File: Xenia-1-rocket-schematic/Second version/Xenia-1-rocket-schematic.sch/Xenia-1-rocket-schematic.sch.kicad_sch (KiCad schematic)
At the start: 0 parts

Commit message: Schematic back to october version
Back to where I was in october, with two sensors
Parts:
- added A?: ADA3708, ADA3708_RPI-ZERO, symbol ADA3708:ADA3708
- added U?: BME280, symbol Rocketry_project:BME280
- added U?: LSM9DS1, symbol Rocketry_project:LSM9DS1
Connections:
- new net: A?.1 (3V3[1]), U?.~ (V_in), U?.~ (V_in)
- new net: A?.3 (GPIO2/SDA), U?.~ (V_in)
- new net: A?.5 (GPIO3/SCL), U?.~ (V_in)
- new net: A?.11 (GPIO17/GEN0), U?.~ (V_in)
- new net: A?.13 (GPIO27/GEN2), U?.~ (V_in)
- new net GND: A?.9 (GND[1]), U?.~ (V_in), U?.~ (V_in)
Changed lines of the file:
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@@
 (kicad_sch (version 20211123) (generator eeschema)
   (paper "A4")
+  (junction (at 180.34 118.11) (diameter 0) (color 0 0 0 0)
+  )
+  (junction (at 163.83 69.85) (diameter 0) (color 0 0 0 0)
+  )
+  (junction (at 168.91 133.35) (diameter 0) (color 0 0 0 0)
+  )
+  (wire (pts (xy 93.98 88.9) (xy 96.52 88.9))
+    (stroke (width 0) (type default) (color 0 0 0 0))
+  )
+  (wire (pts (xy 213.36 125.73) (xy 93.98 125.73))
+    (stroke (width 0) (type default) (color 0 0 0 0))
+  )
+  (wire (pts (xy 88.9 133.35) (xy 88.9 83.82))
+    (stroke (width 0) (type default) (color 0 0 0 0))
+  )
+  (wire (pts (xy 152.4 69.85) (xy 163.83 69.85))
+    (stroke (width 0) (type default) (color 0 0 0 0))
+  )
+  (wire (pts (xy 88.9 83.82) (xy 96.52 83.82))
+    (stroke (width 0) (type default) (color 0 0 0 0))
+  )
+  (wire (pts (xy 91.44 76.2) (xy 96.52 76.2))
+    (stroke (width 0) (type default) (color 0 0 0 0))
+  )
+  (wire (pts (xy 163.83 104.14) (xy 163.83 69.85))
+    (stroke (width 0) (type default) (color 0 0 0 0))
+  )
+  (wire (pts (xy 91.44 129.54) (xy 91.44 86.36))
+    (stroke (width 0) (type default) (color 0 0 0 0))
+  )
+  (wire (pts (xy 201.93 104.14) (xy 201.93 118.11))
+    (stroke (width 0) (type default) (color 0 0 0 0))
+  )
+  (wire (pts (xy 213.36 104.14) (xy 213.36 125.73))
+    (stroke (width 0) (type default) (color 0 0 0 0))
+  )
+  (wire (pts (xy 180.34 118.11) (xy 180.34 133.35))
+    (stroke (width 0) (type default) (color 0 0 0 0))
+  )
+  (wire (pts (xy 180.34 62.23) (xy 180.34 118.11))
+    (stroke (width 0) (type default) (color 0 0 0 0))
+  )
+  (wire (pts (xy 96.52 73.66) (xy 96.52 60.96))
+    (stroke (width 0) (type default) (color 0 0 0 0))
+  )
+  (wire (pts (xy 194.31 104.14) (xy 163.83 104.14))
+    (stroke (width 0) (type default) (color 0 0 0 0))
+  )
+  (wire (pts (xy 184.15 68.58) (xy 87.63 68.58))
+    (stroke (width 0) (type default) (color 0 0 0 0))
+  )
+  (wire (pts (xy 163.83 69.85) (xy 172.72 69.85))
+    (stroke (width 0) (type default) (color 0 0 0 0))
+  )
+  (wire (pts (xy 184.15 62.23) (xy 184.15 68.58))
+    (stroke (width 0) (type default) (color 0 0 0 0))
+  )
+  (wire (pts (xy 152.4 60.96) (xy 152.4 69.85))
+    (stroke (width 0) (type default) (color 0 0 0 0))
+  )
+  (wire (pts (xy 91.44 64.77) (xy 91.44 76.2))
+    (stroke (width 0) (type default) (color 0 0 0 0))
+  )
+  (wire (pts (xy 91.44 86.36) (xy 96.52 86.36))
+    (stroke (width 0) (type default) (color 0 0 0 0))
+  )
+  (wire (pts (xy 96.52 60.96) (xy 152.4 60.96))
+    (stroke (width 0) (type default) (color 0 0 0 0))
+  )
+  (wire (pts (xy 87.63 68.58) (xy 87.63 78.74))
+    (stroke (width 0) (type default) (color 0 0 0 0))
+  )
+  (wire (pts (xy 205.74 104.14) (xy 205.74 129.54))
+    (stroke (width 0) (type default) (color 0 0 0 0))
+  )
+  (wire (pts (xy 191.77 64.77) (xy 91.44 64.77))
+    (stroke (width 0) (type default) (color 0 0 0 0))
+  )
+  (wire (pts (xy 201.93 118.11) (xy 180.34 118.11))
+    (stroke (width 0) (type default) (color 0 0 0 0))
+  )
+  (wire (pts (xy 93.98 125.73) (xy 93.98 88.9))
+    (stroke (width 0) (type default) (color 0 0 0 0))
+  )
+  (wire (pts (xy 168.91 133.35) (xy 88.9 133.35))
+    (stroke (width 0) (type default) (color 0 0 0 0))
+  )
+  (wire (pts (xy 205.74 129.54) (xy 91.44 129.54))
+    (stroke (width 0) (type default) (color 0 0 0 0))
+  )
+  (wire (pts (xy 191.77 62.23) (xy 191.77 64.77))
+    (stroke (width 0) (type default) (color 0 0 0 0))
+  )
+  (wire (pts (xy 87.63 78.74) (xy 96.52 78.74))
+    (stroke (width 0) (type default) (color 0 0 0 0))
+  )
+  (wire (pts (xy 180.34 133.35) (xy 168.91 133.35))
+    (stroke (width 0) (type default) (color 0 0 0 0))
+  )
+  (wire (pts (xy 172.72 69.85) (xy 172.72 62.23))
+    (stroke (width 0) (type default) (color 0 0 0 0))
+  )
+  (symbol (lib_id "Rocketry_project:BME280") (at 180.34 52.07 0) (unit 1)
+    (in_bom yes) (on_board yes) (fields_autoplaced)
+    (property "Reference" "U?" (id 0) (at 202.565 52.5053 0)
+      (effects (font (size 1.27 1.27)) (justify left))
+    )
+    (property "Value" "BME280" (id 1) (at 202.565 55.0422 0)
+      (effects (font (size 1.27 1.27)) (justify left))
+    )
+    (property "Footprint" "" (id 2) (at 180.34 52.07 0)
+      (effects (font (size 1.27 1.27)) hide)
+    )
+    (property "Datasheet" "" (id 3) (at 180.34 52.07 0)
+      (effects (font (size 1.27 1.27)) hide)
+    )
+    (pin "~")
+    (pin "~")
+    (pin "~")
+    (pin "~")
+    (pin "~")
+    (pin "~")
+    (pin "~")
+  )
+  (symbol (lib_id "power:GND") (at 168.91 133.35 0) (unit 1)
+    (in_bom yes) (on_board yes) (fields_autoplaced)
+    (property "Reference" "#PWR?" (id 0) (at 168.91 139.7 0)
+      (effects (font (size 1.27 1.27)) hide)
+    )
+    (property "Value" "GND" (id 1) (at 168.91 137.7934 0))
+    (property "Footprint" "" (id 2) (at 168.91 133.35 0)
+      (effects (font (size 1.27 1.27)) hide)
+    )
+    (property "Datasheet" "" (id 3) (at 168.91 133.35 0)
+      (effects (font (size 1.27 1.27)) hide)
+    )
+    (pin "1")
+  )
+  (symbol (lib_id "ADA3708:ADA3708") (at 119.38 96.52 0) (unit 1)
+    (in_bom yes) (on_board yes) (fields_autoplaced)
+    (property "Reference" "A?" (id 0) (at 119.38 67.4202 0))
+    (property "Value" "ADA3708" (id 1) (at 119.38 69.9571 0))
+    (property "Footprint" "ADA3708_RPI-ZERO" (id 2) (at 119.38 96.52 0)
+      (effects (font (size 1.27 1.27)) (justify left bottom) hide)
+    )
+    (property "Datasheet" "" (id 3) (at 119.38 96.52 0)
+      (effects (font (size 1.27 1.27)) (justify left bottom) hide)
+    )
+    (property "MANUFACTURER" "Raspberry" (id 4) (at 119.38 96.52 0)
+      (effects (font (size 1.27 1.27)) (justify left bottom) hide)
+    )
+    (property "STANDARD" "MAnufactutrer Recommendations" (id 5) (at 119.38 96.52 0)
+      (effects (font (size 1.27 1.27)) (justify left bottom) hide)
+    )
+    (pin "1")
+    (pin "10")
+    (pin "11")
+    (pin "12")
+    (pin "13")
+    (pin "14")
+    (pin "15")
+    (pin "16")
+    (pin "17")
+    (pin "18")
+    (pin "19")
+    (pin "2")
+    (pin "20")
+    (pin "21")
+    (pin "22")
+    (pin "23")
+    (pin "24")
+    (pin "25")
+    (pin "26")
+    (pin "27")
+    (pin "28")
+    (pin "29")
+    (pin "3")
+    (pin "30")
+    (pin "31")
+    (pin "32")
+    (pin "33")
+    (pin "34")
+    (pin "35")
+    (pin "36")
+    (pin "37")
+    (pin "38")
+    (pin "39")
+    (pin "4")
+    (pin "40")
+    (pin "5")
+    (pin "6")
+    (pin "7")
+    (pin "8")
+    (pin "9")
+  )
+  (symbol (lib_id "Rocketry_project:LSM9DS1") (at 198.12 100.33 0) (unit 1)
+    (in_bom yes) (on_board yes) (fields_autoplaced)
+    (property "Reference" "U?" (id 0) (at 213.995 90.4072 0))
+    (property "Value" "LSM9DS1" (id 1) (at 213.995 92.9441 0))
+    (property "Footprint" "" (id 2) (at 204.47 95.25 0)
+      (effects (font (size 1.27 1.27)) hide)
+    )
+    (property "Datasheet" "" (id 3) (at 204.47 95.25 0)
+      (effects (font (size 1.27 1.27)) hide)
+    )
+    (pin "~")
+    (pin "~")
+    (pin "~")
+    (pin "~")
+    (pin "~")
+    (pin "~")
+    (pin "~")
+    (pin "~")
+    (pin "~")
+  )
   (sheet_instances
     (path "/" (page "1"))
   )
+  (symbol_instances
+    (path "/5b534168-8c44-4d39-b8ef-48b6953bd40d"
+      (reference "#PWR?") (unit 1) (value "GND") (footprint "")
+    )
+    (path "/82b31fed-6ca0-41f8-9a54-4771ef08f750"
+      (reference "A?") (unit 1) (value "ADA3708") (footprint "ADA3708_RPI-ZERO")
+    )
+    (path "/46adcbd4-74d0-4c16-b05f-98374f2f3ebf"
+      (reference "U?") (unit 1) (value "BME280") (footprint "")
+    )
+    (path "/ea1947e1-cd2e-46b0-a351-5a513277da19"
+      (reference "U?") (unit 1) (value "LSM9DS1") (footprint "")
+    )
+  )
 )

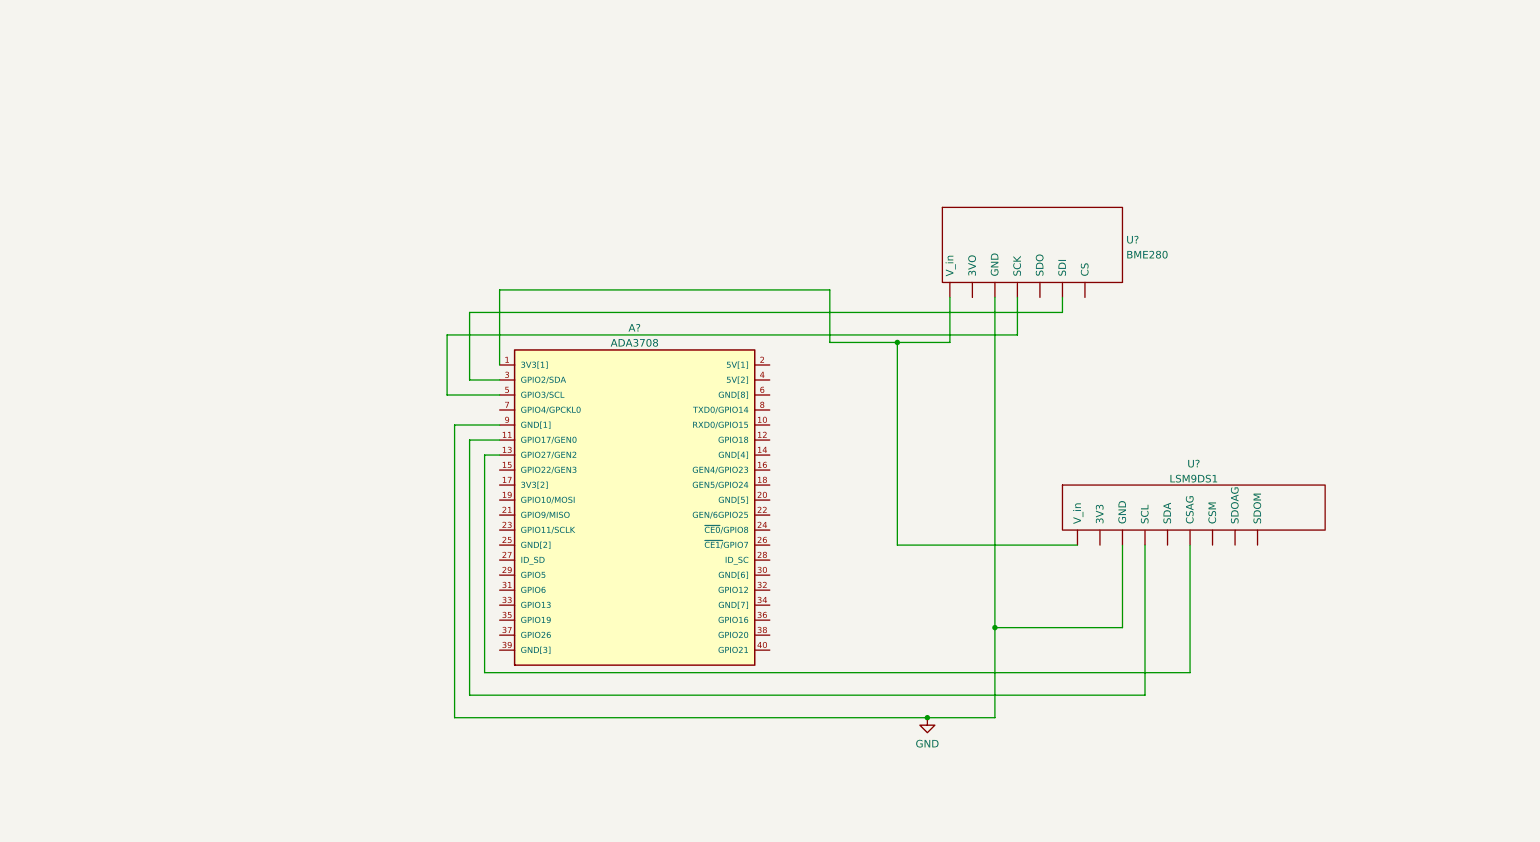
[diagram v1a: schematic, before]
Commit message: Added HX711 HDMI cable and wired it
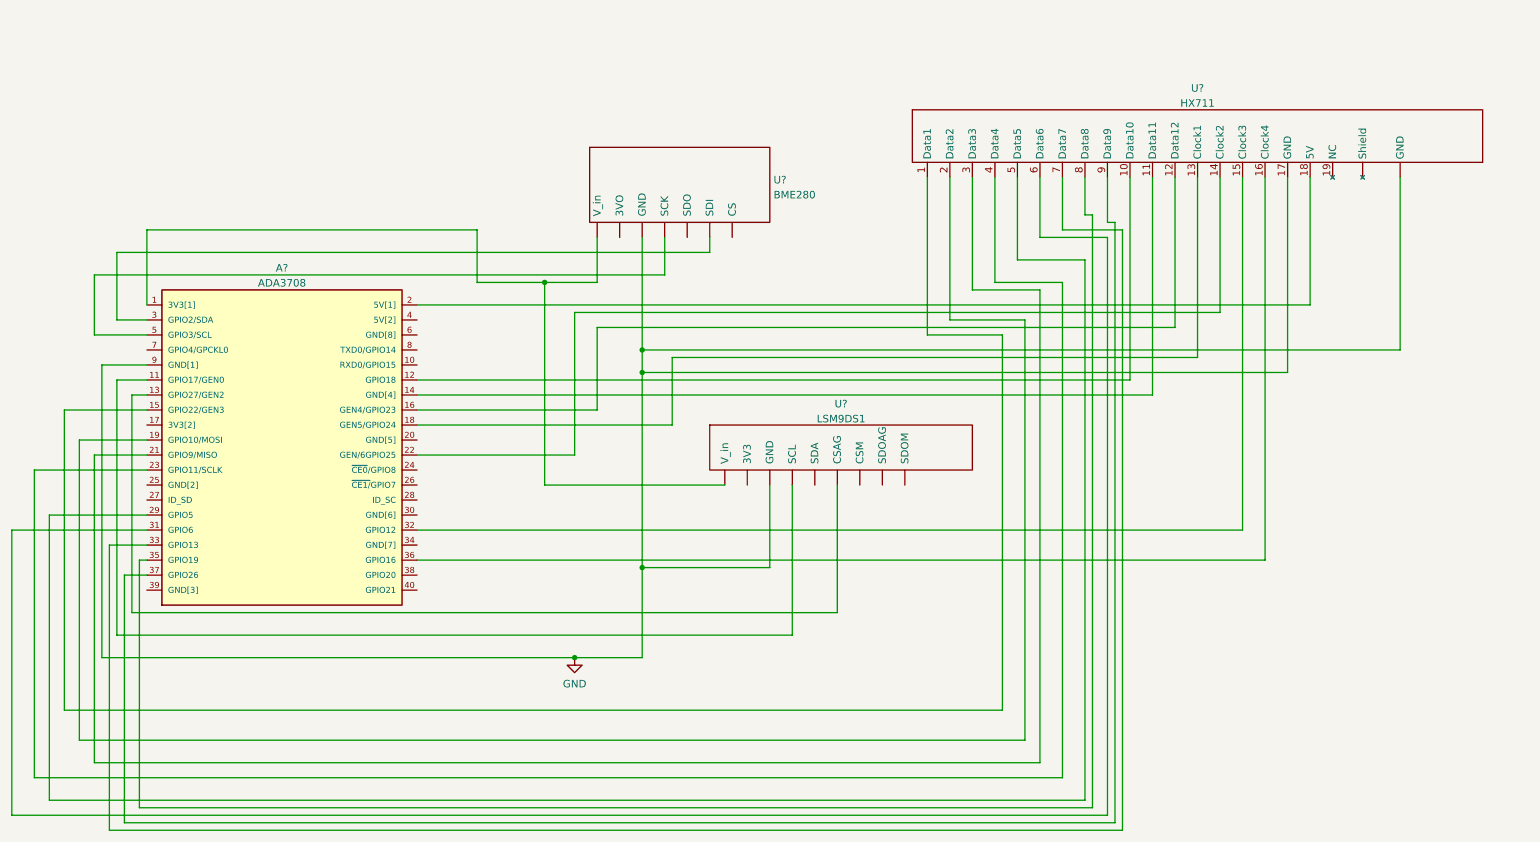
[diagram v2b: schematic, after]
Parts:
- added U?: HX711, symbol Rocketry_project:HX711
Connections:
- net GND: now also U?. (Shield), U?.17 (GND)
- net at A?.12 (GPIO18): now also U?.10 (Data10)
- net at A?.14 (GND[4]): now also U?.11 (Data11)
- net at A?.15 (GPIO22/GEN3): now also U?.1 (Data1)
- net at A?.16 (GEN4/GPIO23): now also U?.12 (Data12)
- net at A?.18 (GEN5/GPIO24): now also U?.13 (Clock1)
- net at A?.19 (GPIO10/MOSI): now also U?.2 (Data2)
- net at A?.2 (5V[1]): now also U?.18 (5V)
- net at A?.21 (GPIO9/MISO): now also U?.3 (Data3)
- net at A?.22 (GEN/6GPIO25): now also U?.14 (Clock2)
- net at A?.23 (GPIO11/SCLK): now also U?.4 (Data4)
- net at A?.29 (GPIO5): now also U?.5 (Data5)
- net at A?.31 (GPIO6): now also U?.6 (Data6)
- net at A?.32 (GPIO12): now also U?.15 (Clock3)
- net at A?.33 (GPIO13): now also U?.7 (Data7)
- net at A?.35 (GPIO19): now also U?.8 (Data8)
- net at A?.36 (GPIO16): now also U?.16 (Clock4)
- net at A?.37 (GPIO26): now also U?.9 (Data9)
- new net: A?.1 (3V3[1]), U?.~ (V_in), U?.~ (V_in)
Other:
- moved on the sheet: A?, U?

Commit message: Changing a list of symbols to labels
Small changes to labels
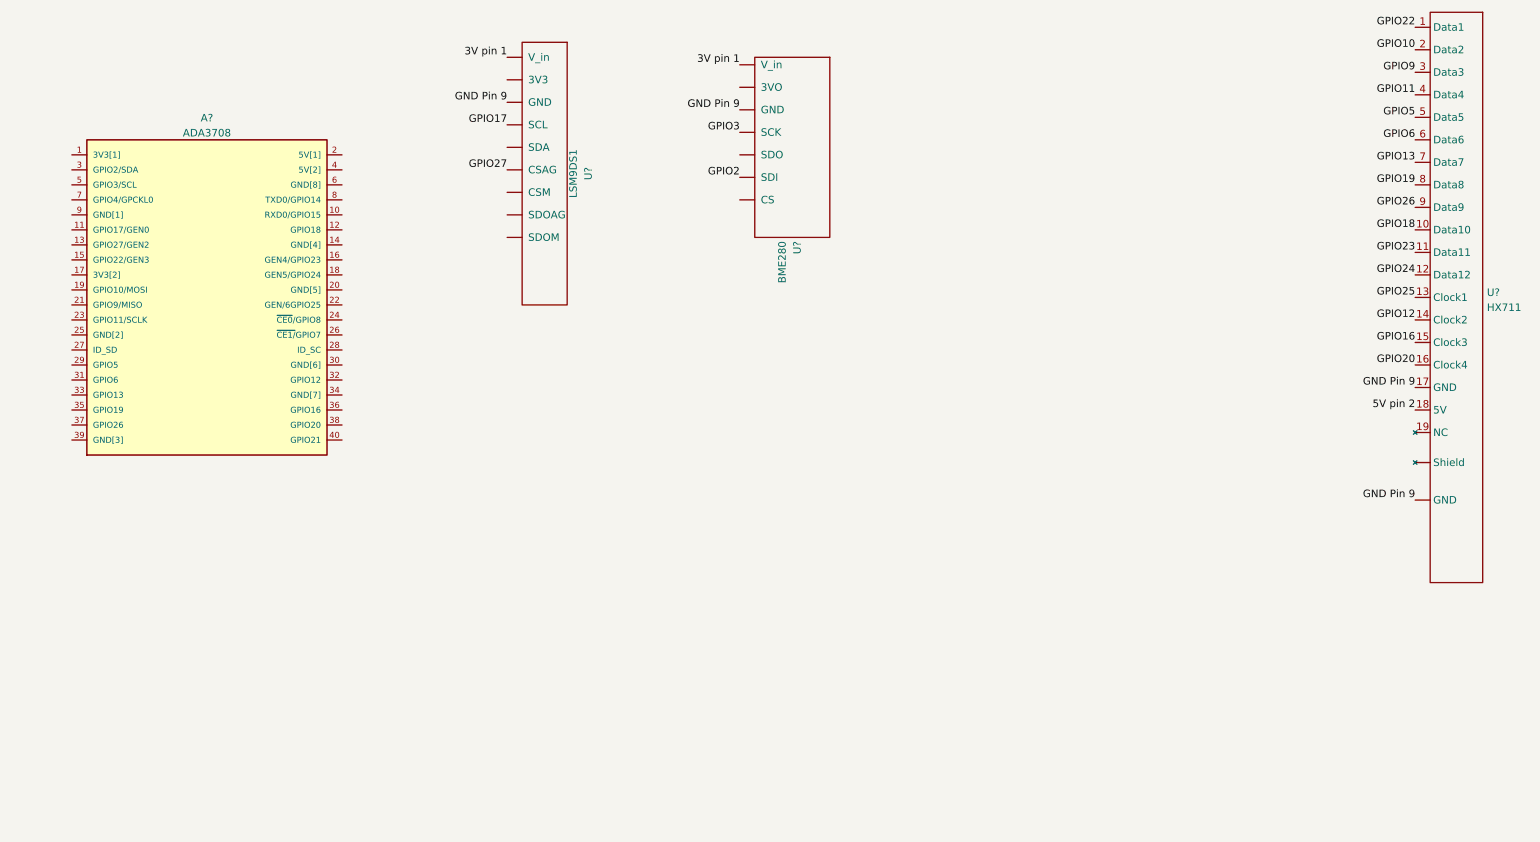
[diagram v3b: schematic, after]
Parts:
- removed A?: ADA3708, ADA3708_RPI-ZERO, symbol ADA3708:ADA3708
- removed U?: BME280, symbol Rocketry_project:BME280
- removed U?: HX711, symbol Rocketry_project:HX711
- removed U?: LSM9DS1, symbol Rocketry_project:LSM9DS1
- added A?: ADA3708, ADA3708_RPI-ZERO, symbol ADA3708:ADA3708
- added U?: LSM9DS1, symbol Rocketry_project:LSM9DS1
- added U?: HX711, symbol Rocketry_project:HX711
- added U?: BME280, symbol Rocketry_project:BME280
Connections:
- new net 3V pin 1: U?.~ (V_in), U?.~ (V_in)
- new net 5V pin 2: U?.18 (5V)
- new net GND Pin 9: U?. (Shield), U?.17 (GND), U?.~ (V_in), U?.~ (V_in)
- new net GPIO10: U?.2 (Data2)
- new net GPIO11: U?.4 (Data4)
- new net GPIO12: U?.14 (Clock2)
- new net GPIO13: U?.7 (Data7)
- new net GPIO16: U?.15 (Clock3)
- new net GPIO17: U?.~ (V_in)
- new net GPIO18: U?.10 (Data10)
- new net GPIO19: U?.8 (Data8)
- new net GPIO2: U?.~ (V_in)
- new net GPIO20: U?.16 (Clock4)
- new net GPIO22: U?.1 (Data1)
- new net GPIO23: U?.11 (Data11)
- new net GPIO24: U?.12 (Data12)
- new net GPIO25: U?.13 (Clock1)
- new net GPIO26: U?.9 (Data9)
- new net GPIO27: U?.~ (V_in)
- new net GPIO3: U?.~ (V_in)
- new net GPIO5: U?.5 (Data5)
- new net GPIO6: U?.6 (Data6)
- new net GPIO9: U?.3 (Data3)
